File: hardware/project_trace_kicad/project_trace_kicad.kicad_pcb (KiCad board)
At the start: 4 copper layers, 100 x 100 mm, 112 parts, among them J204 Screw_Terminal_01x04, J205 Conn_Coaxial, J403 Screw_Terminal_01x04, J601 Conn_01x14_Socket, U201 TLE2426xLP, U202 SN74LVC2G14DBV, U203 AQW280SX, U204 AQW282SX, U205 OPA2837IRUNT, U206 TS5A23159DGS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

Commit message: final(?) Silkscreen
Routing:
- net GND: track 102.3 -> 119.8 mm, vias 143 -> 154

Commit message: Improvements to PCB
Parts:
- added C214: 10u, Capacitor_SMD:C_0805_2012Metric_Pad1.18x1.45mm_HandSolder, B.Cu at (137.1, 128.6)
- C203: value 4u7 -> 10u; footprint Capacitor_THT:CP_Radial_D6.3mm_P2.50mm -> Capacitor_SMD:C_0805_2012Metric_Pad1.18x1.45mm_HandSolder; moved to B.Cu
- R501: value 100 -> 24R9; footprint ProjectTraceFootprints:RN73R2ATTD1000B25 -> Resistor_SMD:R_0603_1608Metric_Pad0.98x0.95mm_HandSolder
- moved C203 29.1 mm to (139.1, 128.6), turned to 90 degrees
- moved C211 4.23 mm to (132.1, 116.6), turned to -90 degrees
- moved U304 2.50 mm to (165.6, 130.3), turned to 90 degrees
- moved R303 1.69 mm to (143.8, 123.3)
- moved R309 1.54 mm to (163.0, 130.6)
- moved TP302 1.14 mm to (158.4, 130.7)
- moved C305 1.06 mm to (164.5, 143.5)
- moved R501 0.85 mm to (146.2, 63.9)
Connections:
- C203 pad 1: VCOM -> Net-(C203-Pad1)
- C203 pad 2: GND -> VCOM
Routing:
- net /Inputs/0dBAtten.~{EN}: track 33.3 -> 137.2 mm, vias 2 -> 3
- net GND: track 119.8 -> 125.1 mm, vias 154 -> 175
- net VCOM: track 144.2 -> 139.9 mm, vias 4 -> 6
- net +3V3: track 277.4 -> 279.8 mm
- net /Inputs/ACCouple.~{EN}: track 37.8 -> 40.0 mm
- net +5V: track 186.8 -> 188.9 mm, vias 14 -> 13
- net +2V5: track 44.6 -> 46.6 mm
- net Net-(C203-Pad1): track 0.00 -> 2.00 mm
- net /Inputs/AttenBuffer: track 23.8 -> 25.6 mm
- net Net-(U302D-+): track 15.5 -> 17.2 mm, vias 1 -> 0
- net Net-(U203A-P1): track 18.4 -> 19.9 mm, vias 0 -> 1
- net Net-(U501C-PC9): track 4.36 -> 5.69 mm
- net Net-(R303-Pad2): track 3.61 -> 4.87 mm
- net +4V: track 15.3 -> 14.3 mm
- net /Inputs/-40dBAtten.~{EN}: track 109.8 -> 110.7 mm
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
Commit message: Improvements to PCB
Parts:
- added R213: 1k, Resistor_SMD:R_0603_1608Metric_Pad0.98x0.95mm_HandSolder, F.Cu at (125.7, 118.5)
- moved C404 1.65 mm to (194.9, 125.1), turned to 90 degrees
- moved TP203 1.23 mm to (125.5, 114.7)
- moved R202 0.84 mm to (119.0, 132.5)
- moved R205 0.77 mm to (123.2, 117.6)
- moved R206 0.73 mm to (123.2, 119.2)
- moved JP204 0.21 mm to (129.6, 122.8)
- moved C323 0.20 mm to (154.9, 143.9)
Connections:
- C205 pad 2: /Inputs/AttenBuffer -> /Inputs/VoltmeterBuffer
- JP204 pad 1: /Inputs/AttenBuffer -> /Inputs/VoltmeterBuffer
- R206 pad 1: /Inputs/AttenBuffer -> /Inputs/AmmeterBuffer
- TP203 pad 1: /Inputs/AttenBuffer -> /Inputs/VoltmeterBuffer
- U205 pad 1: /Inputs/AttenBuffer -> /Inputs/AmmeterBuffer
- U205 pad 8: /Inputs/AttenBuffer -> /Inputs/VoltmeterBuffer
- U205 pad 9: /Inputs/AttenBuffer -> /Inputs/VoltmeterBuffer
- U206 pad 4: /Inputs/AttenBuffer -> /Inputs/VoltmeterBuffer
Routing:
- net /Inputs/AttenBuffer: track 25.6 -> 0.00 mm
- net /Inputs/VoltmeterBuffer: track 0.00 -> 20.2 mm
- net +3V3: track 279.8 -> 284.6 mm
- net GND: track 125.1 -> 129.7 mm, vias 175 -> 252
- net /Inputs/AmmeterBuffer: track 0.00 -> 4.42 mm
- net /Inputs/Attten.20dB: track 16.2 -> 15.0 mm
- net +5V: track 188.9 -> 187.9 mm
- net +2V5: track 46.6 -> 46.0 mm
- net VCOM: track 139.9 -> 139.3 mm
- net /Inputs/Ammeter.EN: track 15.8 -> 16.3 mm
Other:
- board text added: "VB"
- board text removed: "AB"

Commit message: Fix Screw Terminal Clearance Issue
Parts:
- moved J205 0.89 mm to (109.1, 135.6)
- moved J204 0.34 mm to (105.8, 118.2)
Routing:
- net +5V: track 187.9 -> 193.0 mm, vias 13 -> 17
- net /Inputs/Ammeter.In: track 21.8 -> 23.7 mm
- net /Inputs/Voltmeter.In: track 35.9 -> 37.7 mm
- net VCOM: track 139.3 -> 141.1 mm

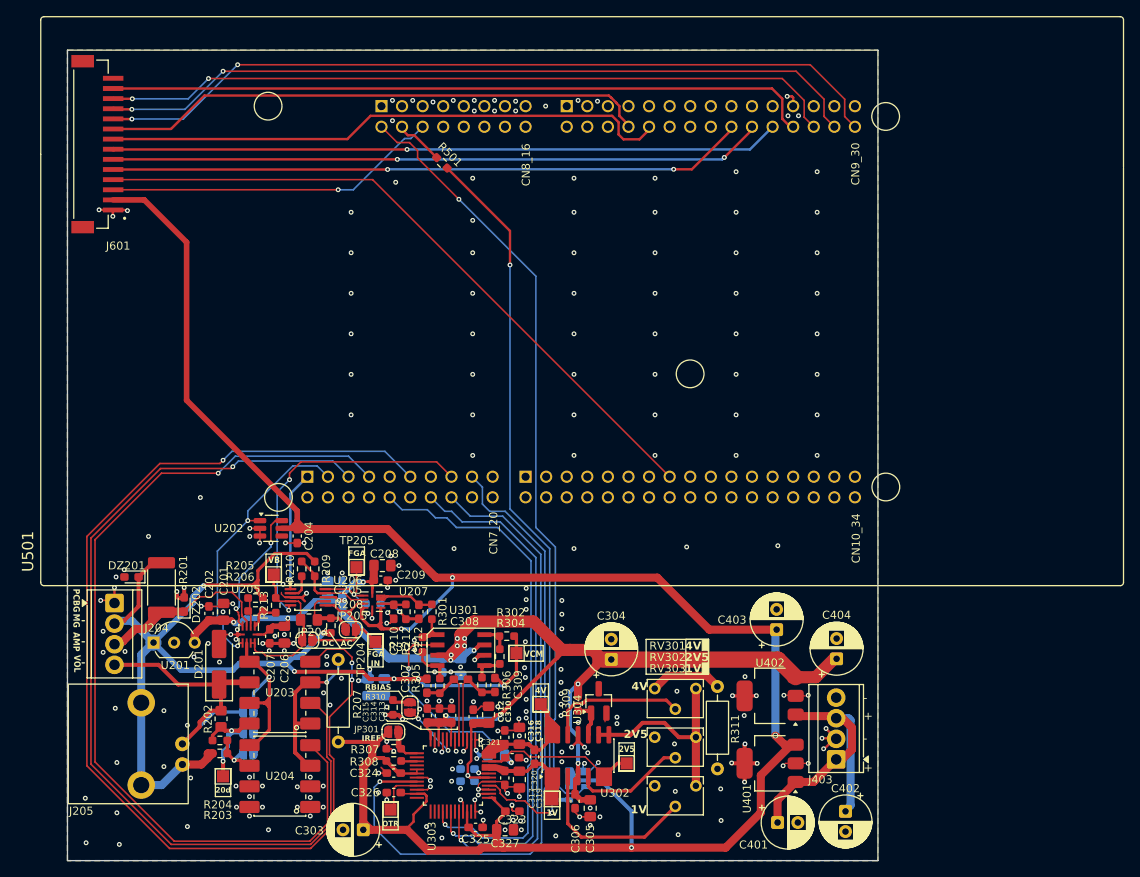
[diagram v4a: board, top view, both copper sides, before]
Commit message: Add Missing Power Connection to Nucleo
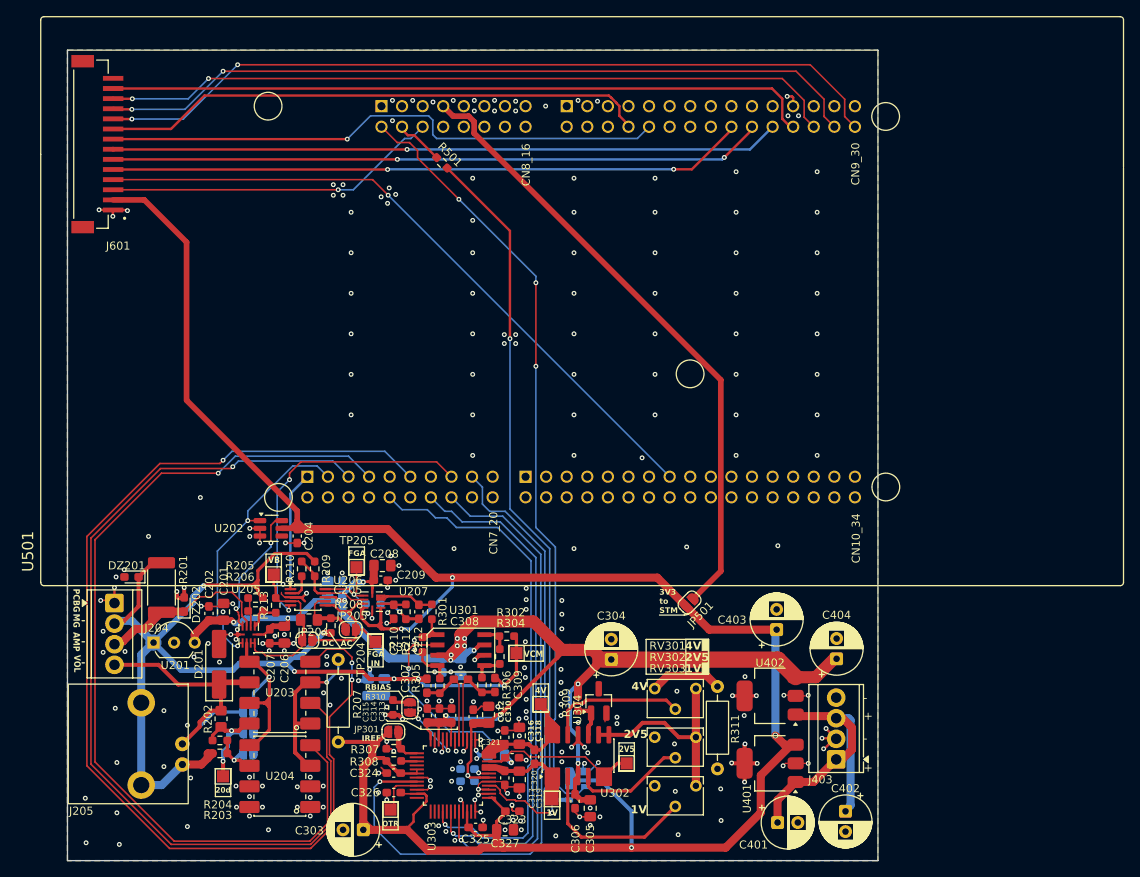
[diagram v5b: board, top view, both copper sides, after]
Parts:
- added JP501: SolderJumper_2_Open, Jumper:SolderJumper-2_P1.3mm_Open_RoundedPad1.0x1.5mm, F.Cu at (176.8, 118.1)
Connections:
- U501 pad 8_7: unconnected-(U501A-3V3-Pad8_7) -> Net-(JP501-B)
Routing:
- net Net-(JP501-B): track 0.00 -> 77.5 mm
- net /Measurement and Analysis Module/SW2: track 69.9 -> 70.1 mm, vias 0 -> 1
- net GND: vias 252 -> 265
- net /Measurement and Analysis Module/SPI3.MOSI: vias 0 -> 1
- net /ADC/CLK.EN: vias 1 -> 3
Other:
- board text added: "3V3 to STM"
